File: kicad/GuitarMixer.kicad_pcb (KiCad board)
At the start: 2 copper layers, 45 x 57.5 mm, 37 parts, among them J1 Conn_01x03_Pin, J2 Conn_01x03_Pin, J3 Conn_01x03_Pin, J4 Conn_01x02_Pin, J5 Conn_01x02_Pin, Q1 2N5457, SW1 SW_SPST, U1 TL072, U2 TL072

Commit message: Fixed slide switch and changed trimmer to pot connection
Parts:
- added J6: Conn_01x03_Pin, Connector_Molex:Molex_KK-254_AE-6410-03A_1x03_P2.54mm_Vertical, F.Cu at (38.8, 81.0)
- D1: value 1N4148 -> 1N5817; footprint Diode_THT:D_DO-35_SOD27_P7.62mm_Horizontal -> Diode_THT:D_DO-41_SOD81_P10.16mm_Horizontal
- moved TR1 34.3 mm to (-0.80, 74.2)
- moved D1 2.65 mm to (56.5, 48.0)
- moved SW1 0.14 mm to (51.4, 50.9)
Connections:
- R11 pad 1: Net-(U2B--) -> Net-(J6-Pin_1)
- R12 pad 1: Net-(R12-Pad1) -> Net-(J6-Pin_3)
- U2 pad 6: Net-(U2B--) -> Net-(J6-Pin_1)
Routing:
- net Net-(U2B--): track 41.6 -> 0.00 mm
- net Net-(J6-Pin_1): track 0.00 -> 33.6 mm
- net Net-(J6-Pin_3): track 0.00 -> 6.91 mm
- net Net-(R12-Pad1): track 6.21 -> 0.00 mm
- net +9VA: track 72.2 -> 70.7 mm
- net Net-(J5-Pin_2): track 49.4 -> 50.1 mm
- net Net-(SW1-B): track 12.7 -> 13.3 mm
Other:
- board text added: "AEGM: Acoustic/Electric Guitar Mixer V0.3 Andrew C.R. Martin (c) 2025"
- board text added: "IN: G El A"
- board text added: "OP: E S"
- board text added: "P: G +"
- board text added: "Vol: H W L"
- board text removed: "AEGM: Acoustic/Electric Guitar Mixer V0.2 Andrew C.R. Martin (c) 2025"
- board text removed: "IN:E El A"
- board text removed: "OUT:E S"
- board text removed: "P:E +"

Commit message: V1.0
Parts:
- removed the REF** at (62.0, 89.0)
- removed the REF** at (25.0, 39.6)
- removed the REF** at (25.0, 89.0)
- removed the REF** at (62.0, 39.6)
- removed TR1: 100K, Potentiometer_THT:Potentiometer_Piher_PT-10-V05_Vertical
- added C10: 10pF, Capacitor_THT:C_Disc_D4.3mm_W1.9mm_P5.00mm, F.Cu at (172.0, 101.2)
- added C11: 100nF, Capacitor_THT:C_Rect_L7.2mm_W2.5mm_P5.00mm_FKS2_FKP2_MKS2_MKP2, F.Cu at (163.7, 92.8)
- added R14: 10K, Resistor_THT:R_Axial_DIN0207_L6.3mm_D2.5mm_P10.16mm_Horizontal, F.Cu at (157.8, 89.5)
- added REF**: MountingHole_3.2mm_M3, MountingHole:MountingHole_3.2mm_M3, F.Cu at (183.9, 79.0)
- added REF**: MountingHole_3.2mm_M3, MountingHole:MountingHole_3.2mm_M3, F.Cu at (119.0, 112.2)
- added REF**: MountingHole_3.2mm_M3, MountingHole:MountingHole_3.2mm_M3, F.Cu at (183.8, 112.1)
- added REF**: MountingHole_3.2mm_M3, MountingHole:MountingHole_3.2mm_M3, F.Cu at (119.0, 79.0)
- C2: footprint Capacitor_THT:C_Disc_D4.7mm_W2.5mm_P5.00mm -> Capacitor_THT:C_Rect_L7.2mm_W2.5mm_P5.00mm_FKS2_FKP2_MKS2_MKP2
- C3: footprint Capacitor_THT:C_Rect_L7.0mm_W3.5mm_P5.00mm -> Capacitor_THT:C_Rect_L7.2mm_W2.5mm_P5.00mm_FKS2_FKP2_MKS2_MKP2
- C4: value 33nF -> 100nF; footprint Capacitor_THT:C_Disc_D4.7mm_W2.5mm_P5.00mm -> Capacitor_THT:C_Rect_L7.2mm_W2.5mm_P5.00mm_FKS2_FKP2_MKS2_MKP2
- C5, C6: value 100nF -> 1uF; footprint Capacitor_THT:C_Rect_L7.0mm_W3.5mm_P5.00mm -> Capacitor_THT:C_Rect_L7.2mm_W4.5mm_P5.00mm_FKS2_FKP2_MKS2_MKP2
- R10, R5, R7: value 100K -> 10K
- moved R5 147.5 mm to (176.2, 86.1)
- moved J6 144.6 mm to (182.1, 100.5), turned to -90 degrees
- moved R10 142.3 mm to (160.2, 110.9), turned to 90 degrees
- moved J2 137.0 mm to (162.4, 80.0), turned to 0 degrees
- moved J5 136.6 mm to (174.2, 80.0)
- moved R12 136.3 mm to (170.4, 97.0), turned to 180 degrees
- moved R13 123.2 mm to (183.6, 96.3)
- moved R6 122.9 mm to (152.8, 97.0)
- moved R11 121.5 mm to (179.9, 96.3)
- moved U2 120.7 mm to (165.8, 105.2)
- moved C5 120.3 mm to (146.5, 79.5), turned to 0 degrees
- moved R4 120.3 mm to (137.2, 92.2), turned to -90 degrees
- moved C3 119.0 mm to (141.4, 85.4), turned to -90 degrees
- moved R7 114.3 mm to (156.6, 100.7), turned to -90 degrees
- moved U1 112.2 mm to (145.6, 85.1)
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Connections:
- net Net-(U2A-+) renamed +4V
- C6 pad 1: Net-(U1B--) -> Net-(C11-Pad2)
- U1 pad 7: Net-(U1B--) -> Net-(C11-Pad2)
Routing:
- net +9VA: track 70.7 -> 171.0 mm
- net Net-(C11-Pad2): track 0.00 -> 39.9 mm
- net Net-(J5-Pin_2): track 50.1 -> 21.2 mm
- net +4V: track 31.8 -> 55.7 mm
- net Earth: track 172.4 -> 192.3 mm
- net Net-(SW1-B): track 13.3 -> 27.9 mm
- net Net-(J6-Pin_1): track 33.6 -> 19.4 mm
- net Net-(J2-Pin_3): track 5.24 -> 19.2 mm
- net Net-(C9-Pad1): track 25.0 -> 38.0 mm
- net Net-(Q1-G): track 22.3 -> 11.5 mm
- net +9V: track 5.16 -> 13.8 mm
- net Net-(J1-Pin_2): track 18.7 -> 10.1 mm
- net Net-(U1B-+): track 27.9 -> 36.4 mm
- net Net-(J6-Pin_3): track 6.91 -> 15.2 mm
- net Net-(J3-Pin_3): track 13.3 -> 8.03 mm
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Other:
- board size 45 x 57.5 mm -> 72.8 x 40.8 mm
- board text added: "+9V G"
- board text added: "10"
- board text added: "5"
- board text added: "A E G"
- board text added: "AEGM"
- board text added: "Acoustic Vol"
- board text added: "Andrew Martin V1.0 (c)10/25"
- board text added: "Electric Vol"
- board text added: "G Out"
- board text added: "Gain"
- board text added: "H W L"
- board text added: "INPUT"
- board text added: "Impedance"
- board text added: "L W H"
- board text added: "OUT"
- board text added: "PWR"
- board text removed: "10M"
- board text removed: "5M"
- board text removed: "A: L W H"
- board text removed: "AEGM: Acoustic/Electric Guitar Mixer V0.3 Andrew C.R. Martin (c) 2025"
- board text removed: "El: H W L"
- board text removed: "IN: G El A"
- board text removed: "OP: E S"
- board text removed: "P: G +"
- board text removed: "Vol: H W L"

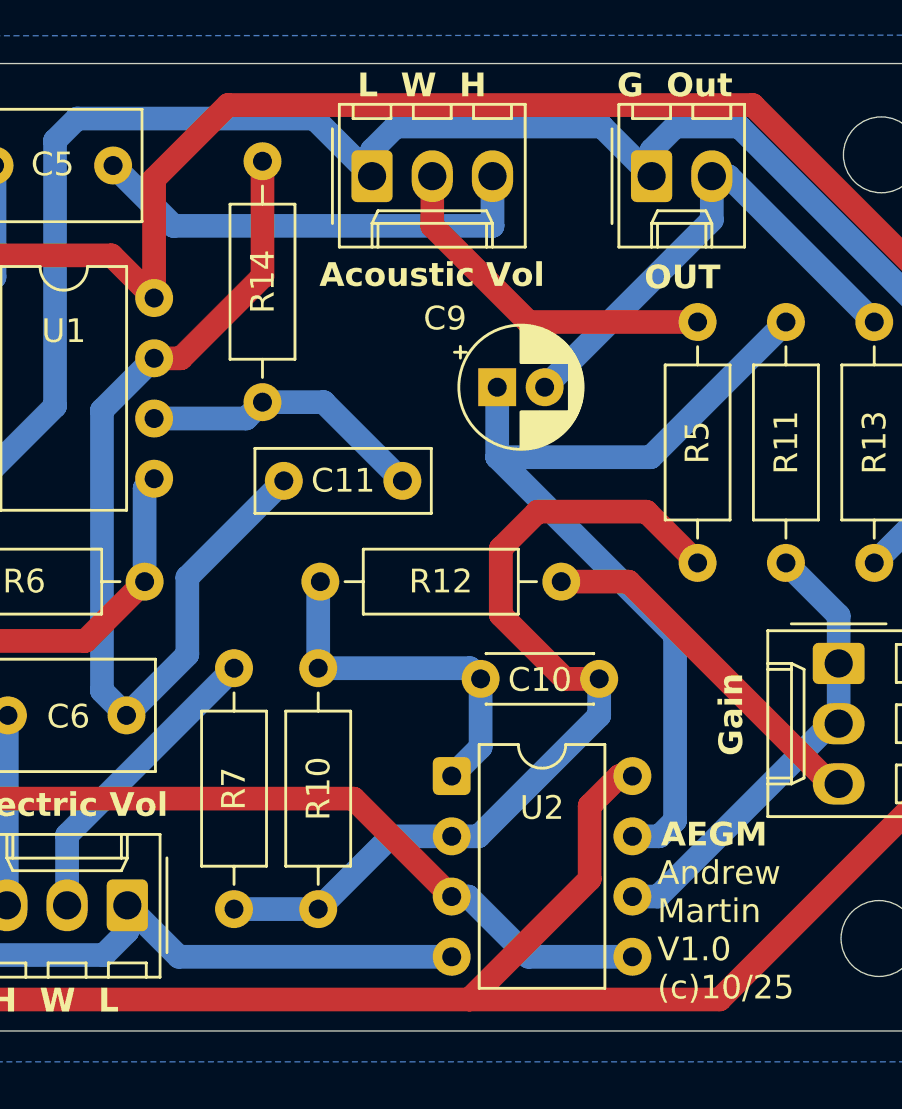
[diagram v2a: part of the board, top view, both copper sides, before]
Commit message: Redid the feedback on the non-inverting amplifier for electric guitar
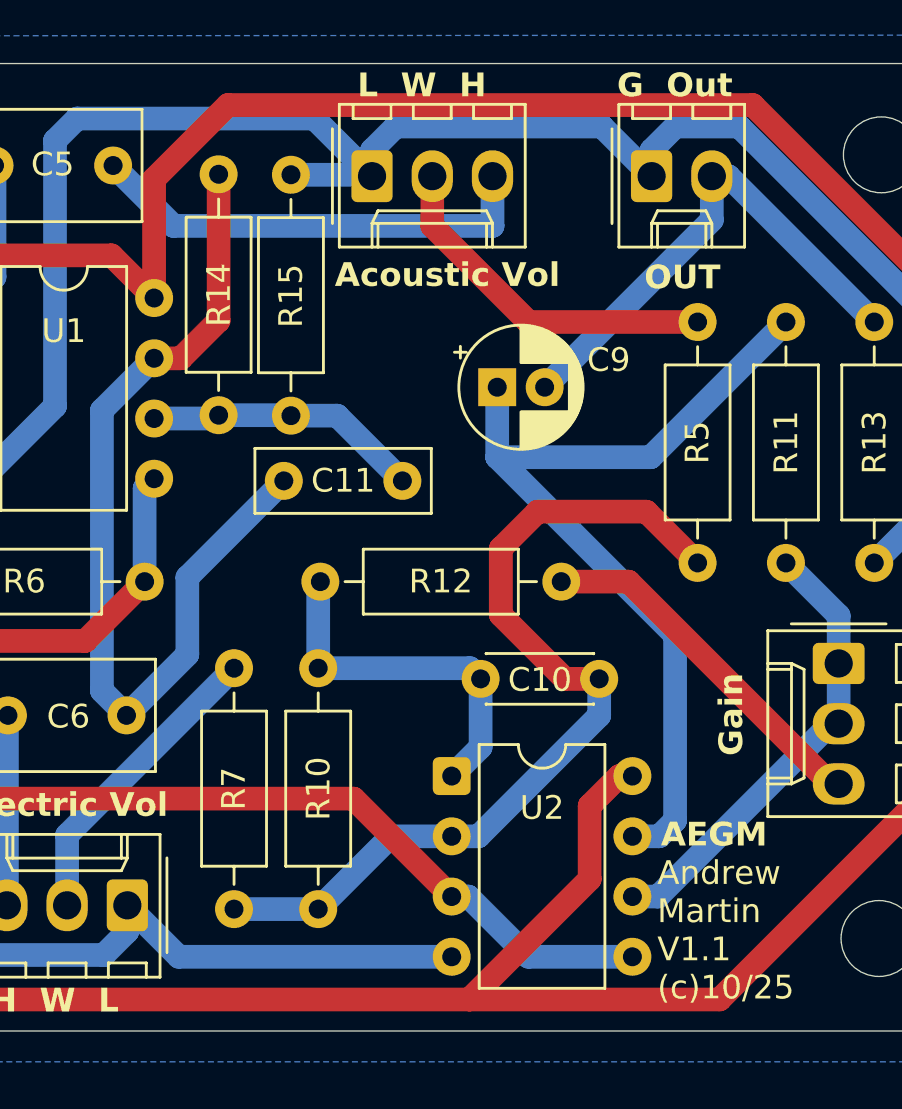
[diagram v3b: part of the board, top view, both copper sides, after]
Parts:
- added R15: 1K, Resistor_THT:R_Axial_DIN0207_L6.3mm_D2.5mm_P10.16mm_Horizontal, F.Cu at (159.0, 90.0)
- R14: value 10K -> 1K
- moved R14 1.93 mm to (155.9, 90.0)
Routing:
- net Earth: track 192.3 -> 195.7 mm
- net Net-(C11-Pad2): track 39.9 -> 38.6 mm
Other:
- board text added: "Andrew Martin V1.1 (c)10/25"
- board text removed: "Andrew Martin V1.0 (c)10/25"

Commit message: Board created
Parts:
- removed C10: 10pF, Capacitor_THT:C_Disc_D4.3mm_W1.9mm_P5.00mm
- removed C11: 100nF, Capacitor_THT:C_Rect_L7.2mm_W2.5mm_P5.00mm_FKS2_FKP2_MKS2_MKP2
- removed C6: 1uF, Capacitor_THT:C_Rect_L7.2mm_W4.5mm_P5.00mm_FKS2_FKP2_MKS2_MKP2
- removed C7: 4.7uF, Capacitor_THT:CP_Radial_D5.0mm_P2.00mm
- removed C8: 22uF, Capacitor_THT:CP_Radial_D5.0mm_P2.00mm
- removed C9: 2.2uF, Capacitor_THT:CP_Radial_D5.0mm_P2.00mm
- removed R10, R12, R7: 10K, Resistor_THT:R_Axial_DIN0207_L6.3mm_D2.5mm_P10.16mm_Horizontal
- removed R11, R8, R9: 100K, Resistor_THT:R_Axial_DIN0207_L6.3mm_D2.5mm_P10.16mm_Horizontal
- removed R13: 1M, Resistor_THT:R_Axial_DIN0207_L6.3mm_D2.5mm_P10.16mm_Horizontal
- removed R14, R15: 1K, Resistor_THT:R_Axial_DIN0207_L6.3mm_D2.5mm_P10.16mm_Horizontal
- removed the REF** at (183.9, 79.0)
- removed the REF** at (119.0, 112.2)
- removed the REF** at (183.8, 112.1)
- removed the REF** at (119.0, 79.0)
- added C101: 1pF, Capacitor_THT:C_Disc_D4.3mm_W1.9mm_P5.00mm, F.Cu at (114.4, 69.3)
- added C102: 4.7nF, Capacitor_THT:C_Rect_L7.2mm_W2.5mm_P5.00mm_FKS2_FKP2_MKS2_MKP2, F.Cu at (114.2, 64.8)
- added C103: 100nF, Capacitor_THT:C_Rect_L7.2mm_W2.5mm_P5.00mm_FKS2_FKP2_MKS2_MKP2, F.Cu at (132.7, 59.0)
- added C104: 100nF, Capacitor_THT:C_Rect_L7.2mm_W2.5mm_P5.00mm_FKS2_FKP2_MKS2_MKP2, F.Cu at (130.6, 76.9)
- added C105: 1uF, Capacitor_THT:C_Rect_L7.2mm_W4.5mm_P5.00mm_FKS2_FKP2_MKS2_MKP2, F.Cu at (145.2, 83.3)
- added C202: 1nF, Capacitor_THT:C_Rect_L7.2mm_W2.5mm_P5.00mm_FKS2_FKP2_MKS2_MKP2, F.Cu at (106.1, 90.7)
- added C203: 100nF, Capacitor_THT:C_Rect_L7.2mm_W2.5mm_P5.00mm_FKS2_FKP2_MKS2_MKP2, F.Cu at (114.9, 90.7)
- added C204: 100nF, Capacitor_THT:C_Rect_L7.2mm_W2.5mm_P5.00mm_FKS2_FKP2_MKS2_MKP2, F.Cu at (149.8, 77.9)
- added C205: 1uF, Capacitor_THT:C_Rect_L7.2mm_W4.5mm_P5.00mm_FKS2_FKP2_MKS2_MKP2, F.Cu at (145.2, 91.5)
- added R1011: 4M7, Resistor_THT:R_Axial_DIN0207_L6.3mm_D2.5mm_P10.16mm_Horizontal, F.Cu at (119.2, 69.0)
- added R1012: 4M7, Resistor_THT:R_Axial_DIN0207_L6.3mm_D2.5mm_P10.16mm_Horizontal, F.Cu at (115.9, 78.3)
- added R102: 220K, Resistor_THT:R_Axial_DIN0207_L6.3mm_D2.5mm_P10.16mm_Horizontal, F.Cu at (125.0, 59.0)
- added R103: 10K, Resistor_THT:R_Axial_DIN0207_L6.3mm_D2.5mm_P10.16mm_Horizontal, F.Cu at (130.1, 66.1)
- added R104: 100K, Resistor_THT:R_Axial_DIN0207_L6.3mm_D2.5mm_P10.16mm_Horizontal, F.Cu at (123.1, 79.2)
- added R105: 100K, Resistor_THT:R_Axial_DIN0207_L6.3mm_D2.5mm_P10.16mm_Horizontal, F.Cu at (130.7, 90.3)
- added R106: 1K, Resistor_THT:R_Axial_DIN0207_L6.3mm_D2.5mm_P10.16mm_Horizontal, F.Cu at (126.9, 82.5)
- added R107: 1K, Resistor_THT:R_Axial_DIN0207_L6.3mm_D2.5mm_P10.16mm_Horizontal, F.Cu at (126.9, 79.2)
- added R108: 10K, Resistor_THT:R_Axial_DIN0207_L6.3mm_D2.5mm_P10.16mm_Horizontal, F.Cu at (130.7, 93.1)
- added R201: 1M, Resistor_THT:R_Axial_DIN0207_L6.3mm_D2.5mm_P10.16mm_Horizontal, F.Cu at (108.5, 94.8)
- added R204: 100K, Resistor_THT:R_Axial_DIN0207_L6.3mm_D2.5mm_P10.16mm_Horizontal, F.Cu at (123.1, 99.4)
- added R205: 100K, Resistor_THT:R_Axial_DIN0207_L6.3mm_D2.5mm_P10.16mm_Horizontal, F.Cu at (108.5, 98.6)
- added R206: 1K, Resistor_THT:R_Axial_DIN0207_L6.3mm_D2.5mm_P10.16mm_Horizontal, F.Cu at (149.7, 80.8)
- added R207: 1K, Resistor_THT:R_Axial_DIN0207_L6.3mm_D2.5mm_P10.16mm_Horizontal, F.Cu at (145.7, 80.2)
- added R208: 10K, Resistor_THT:R_Axial_DIN0207_L6.3mm_D2.5mm_P10.16mm_Horizontal, F.Cu at (144.9, 102.8)
- added REF**: MountingHole_3.2mm_M3, MountingHole:MountingHole_3.2mm_M3, F.Cu at (107.8, 59.7)
- added REF**: MountingHole_3.2mm_M3, MountingHole:MountingHole_3.2mm_M3, F.Cu at (171.3, 105.9)
- added REF**: MountingHole_3.2mm_M3, MountingHole:MountingHole_3.2mm_M3, F.Cu at (171.4, 60.1)
- added REF**: MountingHole_3.2mm_M3, MountingHole:MountingHole_3.2mm_M3, F.Cu at (107.7, 105.9)
- C1: value 1pF -> 10pF
- C2: value 33nF -> 10pF; footprint Capacitor_THT:C_Rect_L7.2mm_W2.5mm_P5.00mm_FKS2_FKP2_MKS2_MKP2 -> Capacitor_THT:C_Disc_D4.3mm_W1.9mm_P5.00mm
- C3: value 100nF -> 2.2uF; footprint Capacitor_THT:C_Rect_L7.2mm_W2.5mm_P5.00mm_FKS2_FKP2_MKS2_MKP2 -> Capacitor_THT:CP_Radial_D5.0mm_P2.00mm
- C4: value 100nF -> 4.7uF; footprint Capacitor_THT:C_Rect_L7.2mm_W2.5mm_P5.00mm_FKS2_FKP2_MKS2_MKP2 -> Capacitor_THT:CP_Radial_D5.0mm_P2.00mm
- C5: value 1uF -> 22uF; footprint Capacitor_THT:C_Rect_L7.2mm_W4.5mm_P5.00mm_FKS2_FKP2_MKS2_MKP2 -> Capacitor_THT:CP_Radial_D5.0mm_P2.00mm
- R1, R2: value 4M7 -> 10K
- R3: value 220K -> 10K
- R4: value 10K -> 1M
- R5: value 10K -> 100K
- R6: value 1M -> 100K
- moved U2 48.1 mm to (150.6, 59.6)
- moved C2 38.2 mm to (165.4, 68.7), turned to 90 degrees
- moved C4 38.1 mm to (155.9, 95.2), turned to -90 degrees
- moved J4 36.9 mm to (157.4, 104.1), turned to 180 degrees
- moved R3 36.7 mm to (161.8, 68.7), turned to 90 degrees
- moved D1 34.0 mm to (160.9, 89.8), turned to 0 degrees
- moved J6 33.6 mm to (163.7, 72.4)
- moved C3 32.0 mm to (171.5, 74.3)
- moved J2 27.6 mm to (135.3, 85.1)
- moved C1 26.0 mm to (147.6, 64.9), turned to 90 degrees
- moved Q1 25.1 mm to (124.8, 65.6)
- moved J1 23.8 mm to (107.3, 72.7)
- moved J3 23.1 mm to (135.2, 94.9), turned to 0 degrees
- moved R4 18.1 mm to (153.6, 84.7), turned to 0 degrees
- moved U1 17.7 mm to (134.6, 71.2)
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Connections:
- C1 pad 1: Net-(J1-Pin_3) -> Net-(U2A--)
- C1 pad 2: Earth -> Net-(C1-Pad2)
- C2 pad 1: Net-(J1-Pin_3) -> Net-(J6-Pin_1)
- C2 pad 2: Net-(Q1-G) -> Net-(C2-Pad2)
- C3 pad 1: Net-(Q1-S) -> Net-(C2-Pad2)
- C3 pad 2: Net-(C3-Pad2) -> Net-(J5-Pin_2)
- C4 pad 1: Net-(J1-Pin_2) -> +9VA
- C4 pad 2: Net-(U1B-+) -> Earth
- C5 pad 1: Net-(U1A--) -> +4V
- C5 pad 2: Net-(J2-Pin_3) -> Earth
- R1 pad 1: Net-(Q1-G) -> Net-(U2A--)
- R1 pad 2: Net-(SW1-B) -> Net-(C1-Pad2)
- R2 pad 1: Net-(SW1-B) -> Net-(J6-Pin_3)
- R2 pad 2: Earth -> Net-(C1-Pad2)
- R3 pad 1: Net-(Q1-S) -> Net-(J6-Pin_1)
- R3 pad 2: Earth -> Net-(C2-Pad2)
- R4 pad 1: Net-(C3-Pad2) -> Earth
- R4 pad 2: Net-(U1A-+) -> Net-(J5-Pin_2)
- R5 pad 1: Net-(J2-Pin_2) -> +4V
- R5 pad 2: Net-(U2A--) -> +9VA
- R6 pad 1: Net-(U1B-+) -> Earth
- R6 pad 2: Earth -> +4V
- U1 pad 1: Net-(U1A--) -> Net-(C104-Pad2)
- U2 pad 1: Net-(C10-Pad2) -> Net-(C1-Pad2)
- U2 pad 7: Net-(C9-Pad1) -> Net-(C2-Pad2)
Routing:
- net Net-(U2A--): track 38.2 -> 116.8 mm
- net Earth: track 195.7 -> 253.8 mm
- net Net-(C9-Pad1): track 38.0 -> 0.00 mm
- net +9VA: track 171.0 -> 140.0 mm
- net Net-(C104-Pad2): track 0.00 -> 27.4 mm
- net Net-(C2-Pad2): track 0.00 -> 25.2 mm
- net Net-(C1-Pad2): track 0.00 -> 21.7 mm
- net +9V: track 13.8 -> 32.4 mm
- net Net-(SW1-B): track 27.9 -> 10.8 mm
- net Net-(U1A-+): track 16.4 -> 33.0 mm
- net Net-(C10-Pad2): track 15.3 -> 0.00 mm
- net Net-(J1-Pin_2): track 10.1 -> 24.1 mm
- net Net-(J2-Pin_3): track 19.2 -> 6.19 mm
- net Net-(C103-Pad2): track 0.00 -> 10.5 mm
- net Net-(C202-Pad2): track 0.00 -> 8.96 mm
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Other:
- board size 72.8 x 40.8 mm -> 73.8 x 56.6 mm
- board text added: "+ -"
- board text added: "5M 10M"
- board text added: "9V Power"
- board text added: "A-Vol"
- board text added: "AEGM V1.2 Andrew Martin, Acramonics, (c) 2026"
- board text added: "E-Vol"
- board text added: "IN"
- board text added: "M G"
- board text added: "Opt"
- board text added: "VOLUME"
- board text added: "if R107"
- board text added: "if R207"
- board text added: "or link"
- board text removed: "+9V G"
- board text removed: "10"
- board text removed: "5"
- board text removed: "AEGM"
- board text removed: "Acoustic Vol"
- board text removed: "Andrew Martin V1.1 (c)10/25"
- board text removed: "Electric Vol"
- board text removed: "G Out"
- board text removed: "Gain"
- board text removed: "INPUT"
- board text removed: "Impedance"
- board text removed: "PWR"
